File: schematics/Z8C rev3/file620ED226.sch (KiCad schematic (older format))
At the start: 21 parts

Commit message: working on sound
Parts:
- U?: symbol 74xx:74HC165 -> Z8C-rev3-rescue:74HC165-74xx
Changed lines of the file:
@@
 $Descr A4 11693 8268
 encoding utf-8
-Sheet 4 6
+Sheet 4 7
 Title "SPI Interface"
 Date "2022-02-18"
@@
 $EndDescr
 $Comp
-L 74xx:74HC165 U?
+L Z8C-rev3-rescue:74HC165-74xx U?
 U 1 1 620ED2DC
 P 3700 1650
+AR Path="/620ED2DC" Ref="U?"  Part="1"
+AR Path="/620ED227/620ED2DC" Ref="U?"  Part="1"
 F 0 "U?" H 3700 2731 50  0000 C CNN
 F 1 "74HC165" H 3700 2640 50  0000 C CNN

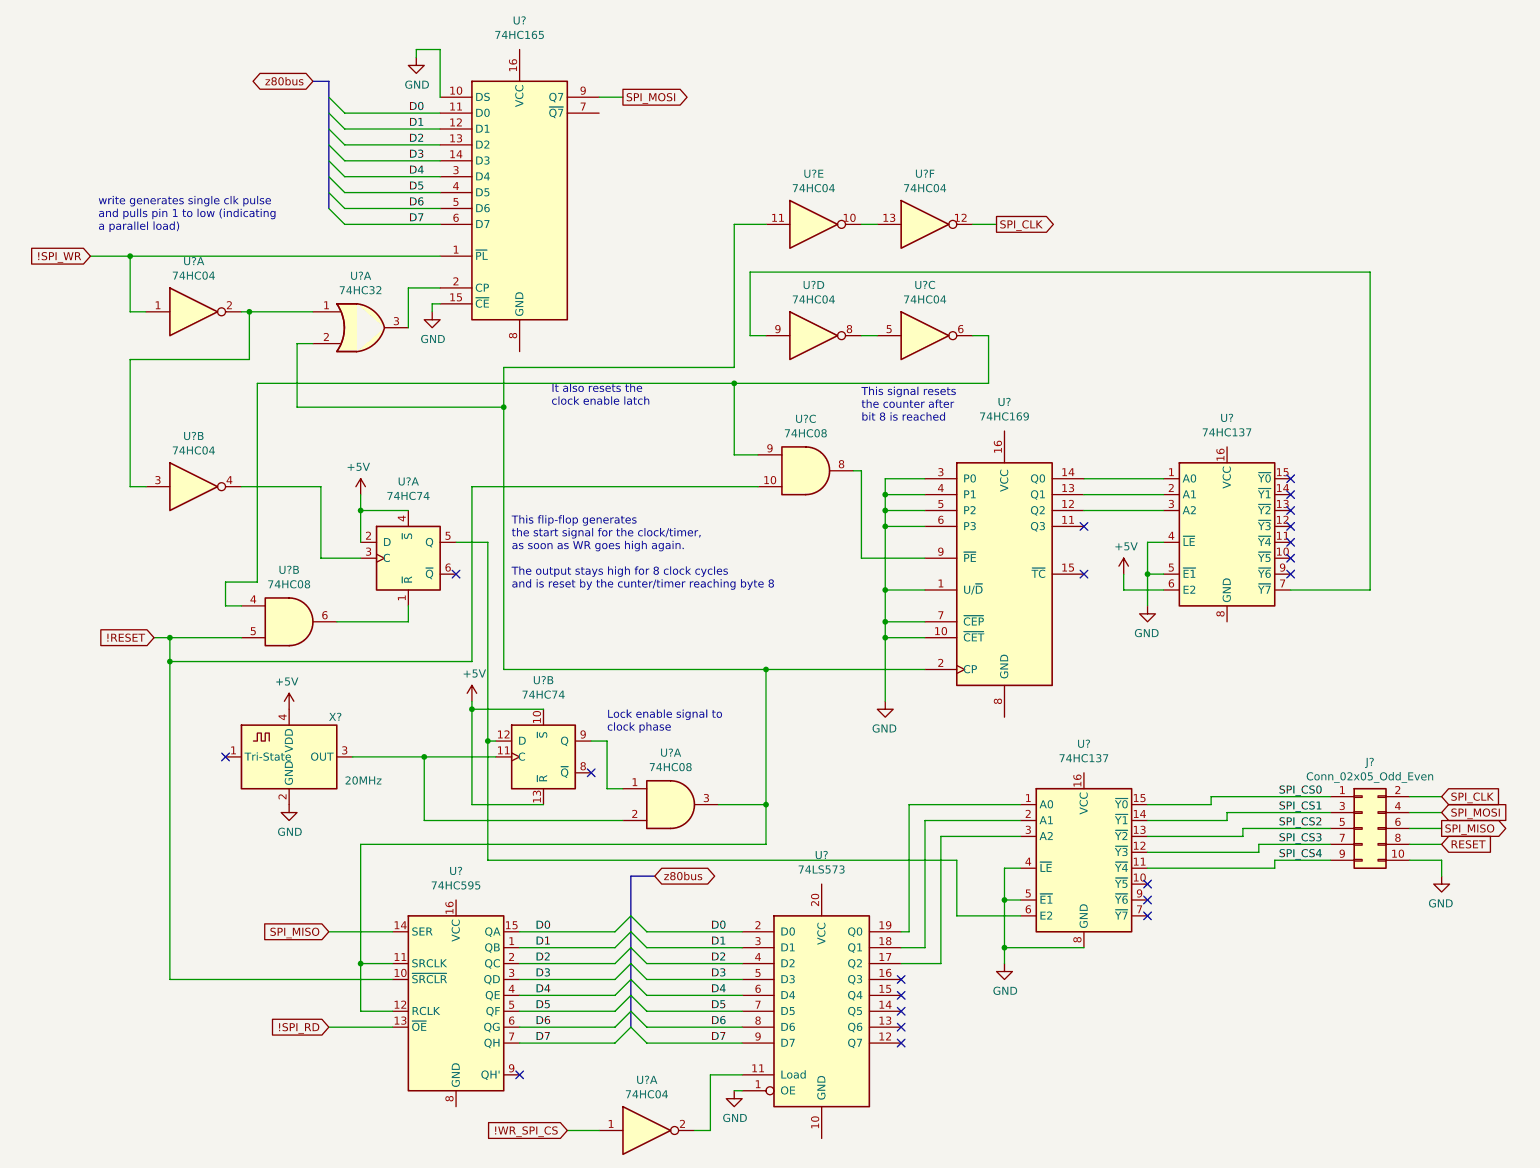
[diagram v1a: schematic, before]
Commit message: added bank switching, apu, dma and IRQ logic. Misc. improvements
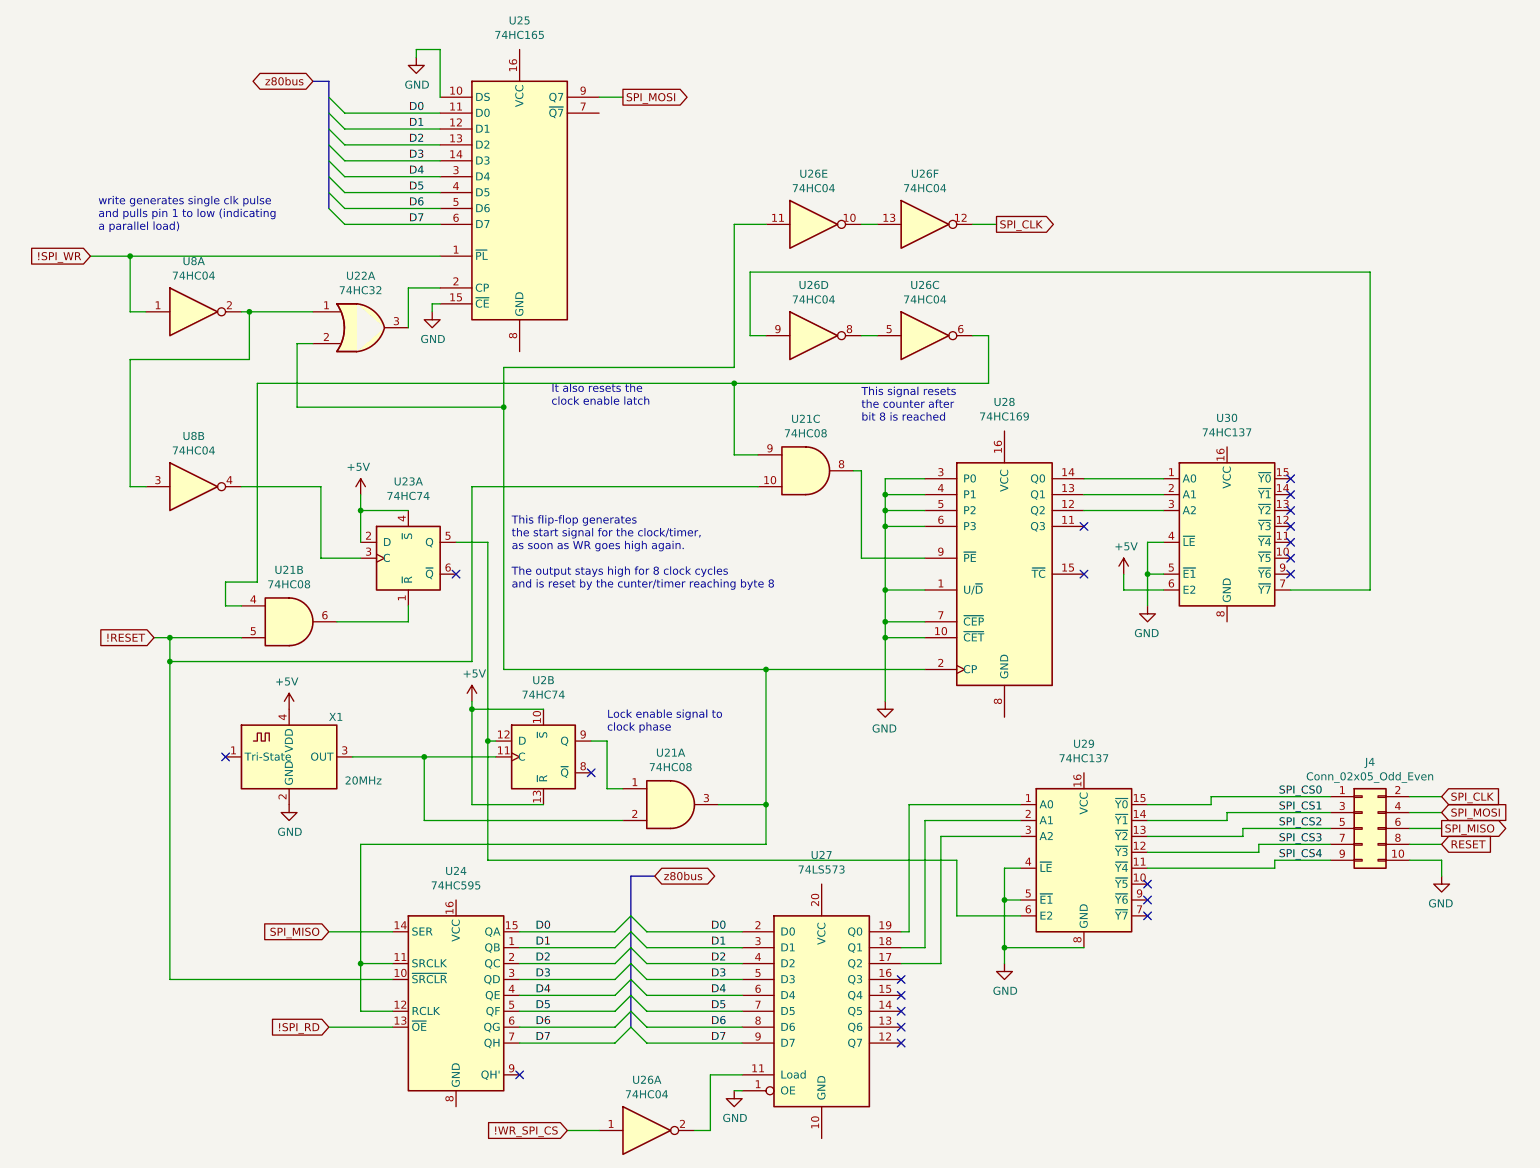
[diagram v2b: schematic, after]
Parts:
- gave numbers to parts that had none: 14
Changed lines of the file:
@@
 P 3700 1650
 AR Path="/620ED2DC" Ref="U?"  Part="1"
-AR Path="/620ED227/620ED2DC" Ref="U?"  Part="1"
-F 0 "U?" H 3700 2731 50  0000 C CNN
+AR Path="/620ED227/620ED2DC" Ref="U25"  Part="1"
+F 0 "U25" H 3700 2731 50  0000 C CNN
 F 1 "74HC165" H 3700 2640 50  0000 C CNN
 F 2 "" H 3700 1650 50  0001 C CNN
@@
 D7
 $Comp
-L power:GND #PWR?
+L power:GND #PWR0123
 U 1 1 620F48CD
 P 3150 2400
-F 0 "#PWR?" H 3150 2150 50  0001 C CNN
+F 0 "#PWR0123" H 3150 2150 50  0001 C CNN
 F 1 "GND" H 3155 2227 50  0000 C CNN
 F 2 "" H 3150 2400 50  0001 C CNN
@@
 !SPI_WR
 $Comp
-L power:GND #PWR?
+L power:GND #PWR0124
 U 1 1 620F5443
 P 3050 800
-F 0 "#PWR?" H 3050 550 50  0001 C CNN
+F 0 "#PWR0124" H 3050 550 50  0001 C CNN
 F 1 "GND" H 3055 627 50  0000 C CNN
 F 2 "" H 3050 800 50  0001 C CNN
@@
 	3050 750  3050 800
 $Comp
-L 74xx:74LS32 U?
+L 74xx:74LS32 U22
 U 1 1 620F6E46
 P 2700 2500
-F 0 "U?" H 2700 2825 50  0000 C CNN
+F 0 "U22" H 2700 2825 50  0000 C CNN
 F 1 "74HC32" H 2700 2734 50  0000 C CNN
 F 2 "" H 2700 2500 50  0001 C CNN
@@
 $EndComp
 $Comp
-L 74xx:74HC04 U?
+L 74xx:74HC04 U8
 U 1 1 620FAAEF
 P 1650 2400
-F 0 "U?" H 1650 2717 50  0000 C CNN
+F 0 "U8" H 1650 2717 50  0000 C CNN
 F 1 "74HC04" H 1650 2626 50  0000 C CNN
 F 2 "" H 1650 2400 50  0001 C CNN
@@
 write generates single clk pulse \nand pulls pin 1 to low (indicating \na parallel load)\n
 $Comp
-L 74xx:74HC74 U?
+L 74xx:74HC74 U23
 U 1 1 62104FE5
 P 3000 3950
-F 0 "U?" H 3000 4431 50  0000 C CNN
+F 0 "U23" H 3000 4431 50  0000 C CNN
 F 1 "74HC74" H 3000 4340 50  0000 C CNN
 F 2 "" H 3000 3950 50  0001 C CNN
@@
 $EndComp
 $Comp
-L Oscillator:ASCO X?
+L Oscillator:ASCO X1
 U 1 1 62107221
 P 2250 5200
-F 0 "X?" H 2500 5450 50  0000 L CNN
+F 0 "X1" H 2500 5450 50  0000 L CNN
 F 1 "20MHz" H 2600 5050 50  0000 L CNN
 F 2 "Oscillator:Oscillator_SMD_Abracon_ASCO-4Pin_1.6x1.2mm" H 2350 4850 50  0001 C CNN
@@
 $EndComp
 $Comp
-L 74xx:74HC04 U?
+L 74xx:74HC04 U8
 U 2 1 6210C461
 P 1650 3500
-F 0 "U?" H 1650 3817 50  0000 C CNN
+F 0 "U8" H 1650 3817 50  0000 C CNN
 F 1 "74HC04" H 1650 3726 50  0000 C CNN
 F 2 "" H 1650 3500 50  0001 C CNN
@@
 This flip-flop generates \nthe start signal for the clock/timer, \nas soon as WR goes high again.\n\nThe output stays high for 8 clock cycles \nand is reset by the cunter/timer reaching byte 8
 $Comp
-L 74xx:74HC74 U?
+L 74xx:74HC74 U2
 U 2 1 6211E9AB
 P 3850 5200
-F 0 "U?" H 3850 5681 50  0000 C CNN
+F 0 "U2" H 3850 5681 50  0000 C CNN
 F 1 "74HC74" H 3850 5590 50  0000 C CNN
 F 2 "" H 3850 5200 50  0001 C CNN
@@
 	2650 5200 3100 5200
 $Comp
-L power:+5V #PWR?
+L power:+5V #PWR0125
 U 1 1 62126B17
 P 2700 3550
-F 0 "#PWR?" H 2700 3400 50  0001 C CNN
+F 0 "#PWR0125" H 2700 3400 50  0001 C CNN
 F 1 "+5V" H 2715 3723 50  0000 C CNN
 F 2 "" H 2700 3550 50  0001 C CNN
@@
 $EndComp
 $Comp
-L power:+5V #PWR?
+L power:+5V #PWR0126
 U 1 1 62127243
 P 3400 4850
-F 0 "#PWR?" H 3400 4700 50  0001 C CNN
+F 0 "#PWR0126" H 3400 4700 50  0001 C CNN
 F 1 "+5V" H 3415 5023 50  0000 C CNN
 F 2 "" H 3400 4850 50  0001 C CNN
@@
 	2700 3850 2700 3650
 $Comp
-L power:+5V #PWR?
+L power:+5V #PWR0127
 U 1 1 6212DE9E
 P 2250 4900
-F 0 "#PWR?" H 2250 4750 50  0001 C CNN
+F 0 "#PWR0127" H 2250 4750 50  0001 C CNN
 F 1 "+5V" H 2265 5073 50  0000 C CNN
 F 2 "" H 2250 4900 50  0001 C CNN
@@
 $EndComp
 $Comp
-L power:GND #PWR?
+L power:GND #PWR0128
 U 1 1 6212E3E7
 P 2250 5500
-F 0 "#PWR?" H 2250 5250 50  0001 C CNN
+F 0 "#PWR0128" H 2250 5250 50  0001 C CNN
 F 1 "GND" H 2255 5327 50  0000 C CNN
 F 2 "" H 2250 5500 50  0001 C CNN
@@
 	2300 2600 2400 2600
 $Comp
-L 74xx:74LS169 U?
+L 74xx:74LS169 U28
 U 1 1 6215982F
 P 6750 4050
-F 0 "U?" H 6750 5131 50  0000 C CNN
+F 0 "U28" H 6750 5131 50  0000 C CNN
 F 1 "74HC169" H 6750 5040 50  0000 C CNN
 F 2 "" H 6750 4050 50  0001 C CNN
@@
 NoConn ~ 4150 5300
 $Comp
-L power:GND #PWR?
+L power:GND #PWR0129
 U 1 1 62178D71
 P 6000 4850
-F 0 "#PWR?" H 6000 4600 50  0001 C CNN
+F 0 "#PWR0129" H 6000 4600 50  0001 C CNN
 F 1 "GND" H 6005 4677 50  0000 C CNN
 F 2 "" H 6000 4850 50  0001 C CNN
@@
 	6000 4450 6000 4850
 $Comp
-L 74xx:74HC04 U?
+L 74xx:74HC04 U26
 U 3 1 62190968
 P 6250 2550
-F 0 "U?" H 6250 2867 50  0000 C CNN
+F 0 "U26" H 6250 2867 50  0000 C CNN
 F 1 "74HC04" H 6250 2776 50  0000 C CNN
 F 2 "" H 6250 2550 50  0001 C CNN
@@
 	3000 4350 3000 4250
 $Comp
-L 74xx:74HC137 U?
+L 74xx:74HC137 U30
 U 1 1 621A117E
 P 8150 3850
-F 0 "U?" H 8150 4631 50  0000 C CNN
+F 0 "U30" H 8150 4631 50  0000 C CNN
 F 1 "74HC137" H 8150 4540 50  0000 C CNN
 F 2 "" H 8150 3850 50  0001 C CNN
@@
 $EndComp
 $Comp
-L power:GND #PWR?
+L power:GND #PWR0130
 U 1 1 621A831F
 P 7650 4250
-F 0 "#PWR?" H 7650 4000 50  0001 C CNN
+F 0 "#PWR0130" H 7650 4000 50  0001 C CNN
 F 1 "GND" H 7655 4077 50  0000 C CNN
 F 2 "" H 7650 4250 50  0001 C CNN
@@
 $EndComp
 $Comp
-L power:+5V #PWR?
+L power:+5V #PWR0131
 U 1 1 621A9028
 P 7500 4050
-F 0 "#PWR?" H 7500 3900 50  0001 C CNN
+F 0 "#PWR0131" H 7500 3900 50  0001 C CNN
 F 1 "+5V" H 7515 4223 50  0000 C CNN
 F 2 "" H 7500 4050 50  0001 C CNN
@@
 NoConn ~ 8550 3450
 $Comp
-L 74xx:74HC04 U?
+L 74xx:74HC04 U26
 U 4 1 621BF569
 P 5550 2550
-F 0 "U?" H 5550 2867 50  0000 C CNN
+F 0 "U26" H 5550 2867 50  0000 C CNN
 F 1 "74HC04" H 5550 2776 50  0000 C CNN
 F 2 "" H 5550 2550 50  0001 C CNN
@@
 It also resets the\nclock enable latch
 $Comp
-L 74xx:74HC04 U?
+L 74xx:74HC04 U26
 U 5 1 621CFC59
 P 5550 1850
-F 0 "U?" H 5550 2167 50  0000 C CNN
+F 0 "U26" H 5550 2167 50  0000 C CNN
 F 1 "74HC04" H 5550 2076 50  0000 C CNN
 F 2 "" H 5550 1850 50  0001 C CNN
@@
 $EndComp
 $Comp
-L 74xx:74HC04 U?
+L 74xx:74HC04 U26
 U 6 1 621D0BB8
 P 6250 1850
-F 0 "U?" H 6250 2167 50  0000 C CNN
+F 0 "U26" H 6250 2167 50  0000 C CNN
 F 1 "74HC04" H 6250 2076 50  0000 C CNN
 F 2 "" H 6250 1850 50  0001 C CNN
@@
 	3600 4650 5250 4650
 $Comp
-L 74xx:74LS08 U?
+L 74xx:74LS08 U21
 U 1 1 621F1518
 P 4650 5500
-F 0 "U?" H 4650 5825 50  0000 C CNN
+F 0 "U21" H 4650 5825 50  0000 C CNN
 F 1 "74HC08" H 4650 5734 50  0000 C CNN
 F 2 "" H 4650 5500 50  0001 C CNN
@@
 	5250 4650 6250 4650
 $Comp
-L 74xx:74HC595 U?
+L 74xx:74HC595 U24
 U 1 1 622068AA
 P 3300 6700
-F 0 "U?" H 3300 7481 50  0000 C CNN
+F 0 "U24" H 3300 7481 50  0000 C CNN
 F 1 "74HC595" H 3300 7390 50  0000 C CNN
 F 2 "" H 3300 6700 50  0001 C CNN
@@
 Connection ~ 5250 5500
 $Comp
-L 74xx:74LS08 U?
+L 74xx:74LS08 U21
 U 2 1 622342F0
 P 2250 4350
-F 0 "U?" H 2250 4675 50  0000 C CNN
+F 0 "U21" H 2250 4675 50  0000 C CNN
 F 1 "74HC08" H 2250 4584 50  0000 C CNN
 F 2 "" H 2250 4350 50  0001 C CNN
@@
 	2050 2850 5050 2850
 $Comp
-L 74xx:74LS08 U?
+L 74xx:74LS08 U21
 U 3 1 622985DF
 P 5500 3400
-F 0 "U?" H 5500 3725 50  0000 C CNN
+F 0 "U21" H 5500 3725 50  0000 C CNN
 F 1 "74HC08" H 5500 3634 50  0000 C CNN
 F 2 "" H 5500 3400 50  0001 C CNN
@@
 NoConn ~ 3700 7200
 $Comp
-L 74xx:74LS573 U?
+L 74xx:74LS573 U27
 U 1 1 62327306
 P 5600 6800
-F 0 "U?" H 5600 7781 50  0000 C CNN
+F 0 "U27" H 5600 7781 50  0000 C CNN
 F 1 "74LS573" H 5600 7690 50  0000 C CNN
 F 2 "" H 5600 6800 50  0001 C CNN
@@
 	5050 7300 5100 7300
 $Comp
-L power:GND #PWR?
+L power:GND #PWR0132
 U 1 1 62389FA6
 P 5050 7300
-F 0 "#PWR?" H 5050 7050 50  0001 C CNN
+F 0 "#PWR0132" H 5050 7050 50  0001 C CNN
 F 1 "GND" H 5055 7127 50  0000 C CNN
 F 2 "" H 5050 7300 50  0001 C CNN
@@
 $EndComp
 $Comp
-L 74xx:74HC04 U?
+L 74xx:74HC04 U26
 U 1 1 62396D19
 P 4500 7550
-F 0 "U?" H 4500 7867 50  0000 C CNN
+F 0 "U26" H 4500 7867 50  0000 C CNN
 F 1 "74HC04" H 4500 7776 50  0000 C CNN
 F 2 "" H 4500 7550 50  0001 C CNN
@@
 	4900 7200 5100 7200
 $Comp
-L 74xx:74HC137 U?
+L 74xx:74HC137 U29
 U 1 1 623B1537
 P 7250 5900
-F 0 "U?" H 7250 6681 50  0000 C CNN
+F 0 "U29" H 7250 6681 50  0000 C CNN
 F 1 "74HC137" H 7250 6590 50  0000 C CNN
 F 2 "" H 7250 5900 50  0001 C CNN
@@
 Connection ~ 3500 5100
 $Comp
-L power:GND #PWR?
+L power:GND #PWR0133
 U 1 1 623E7392
 P 6750 6500
-F 0 "#PWR?" H 6750 6250 50  0001 C CNN
+F 0 "#PWR0133" H 6750 6250 50  0001 C CNN
 F 1 "GND" H 6755 6327 50  0000 C CNN
 F 2 "" H 6750 6500 50  0001 C CNN
@@
 	6750 6400 6750 6100
 $Comp
-L Connector_Generic:Conn_02x05_Odd_Even J?
+L Connector_Generic:Conn_02x05_Odd_Even J4
 U 1 1 6242D84B
 P 9000 5650
-F 0 "J?" H 9050 6067 50  0000 C CNN
+F 0 "J4" H 9050 6067 50  0000 C CNN
 F 1 "Conn_02x05_Odd_Even" H 9050 5976 50  0000 C CNN
 F 2 "" H 9000 5650 50  0001 C CNN
@@
 SPI_MISO
 $Comp
-L power:GND #PWR?
+L power:GND #PWR0134
 U 1 1 6243040B
 P 9500 5950
-F 0 "#PWR?" H 9500 5700 50  0001 C CNN
+F 0 "#PWR0134" H 9500 5700 50  0001 C CNN
 F 1 "GND" H 9505 5777 50  0000 C CNN
 F 2 "" H 9500 5950 50  0001 C CNN
